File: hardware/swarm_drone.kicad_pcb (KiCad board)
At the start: 4 copper layers, 45 x 45 mm, 103 parts, among them J1 Conn_01x02_Pin, J2 Conn_01x03_Socket, J3 Conn_01x03_Socket, J5 Conn_01x02_Socket, J6 Conn_01x02_Socket, J7 Conn_01x02_Socket, J8 Conn_01x02_Socket, Q1 AO3400A, Q2 AO3400A, Q3 AO3400A, Q4 AO3400A, SW1 SW_Push, U1 STM32F405RGT7, U2 TPS7A91, U3 ICM-42688-P, U4 BMP581, U5 VL53L1CXV0FY1, U6 GD25Q128ESIGR, U7 nRF24L01P, X1 8MHz, Y1 16MHz (C13738)

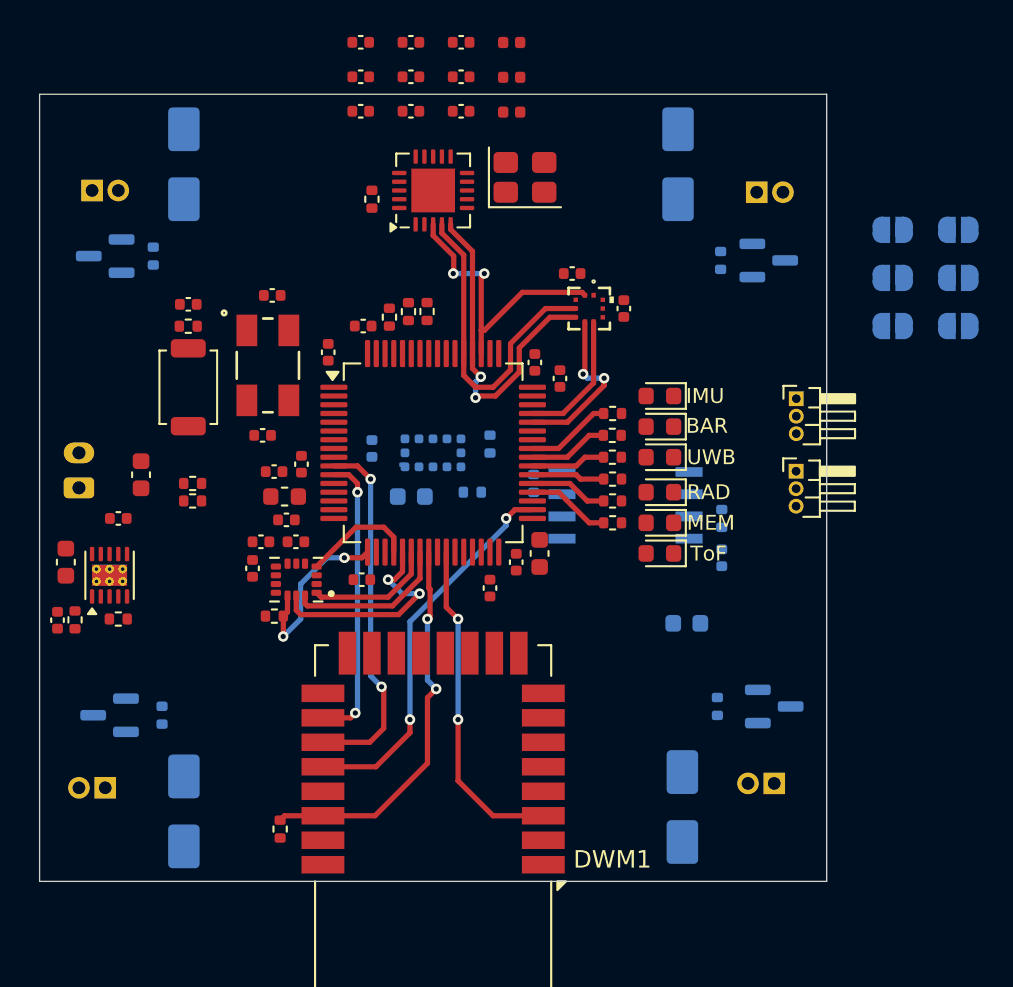
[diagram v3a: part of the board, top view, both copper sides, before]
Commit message: feat(kicad): Rerouted board and changed nets to provide ease in routing
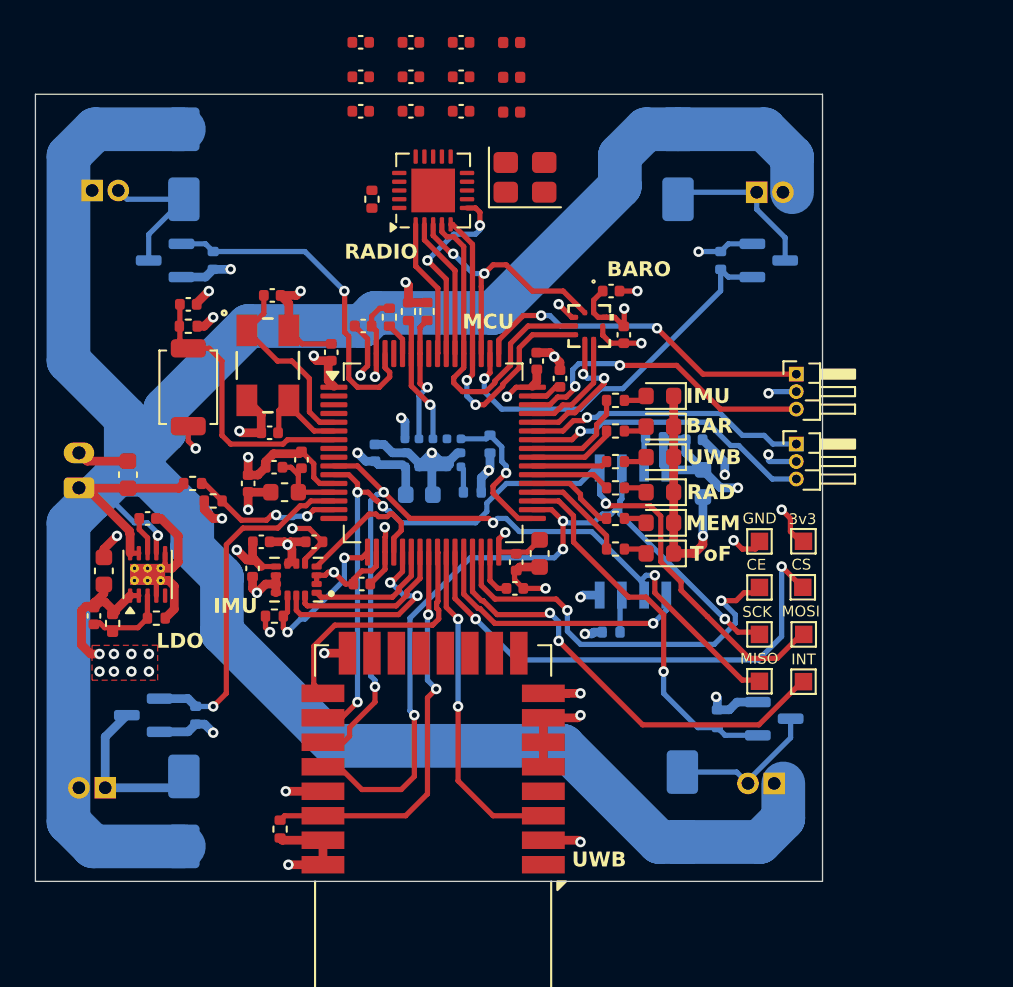
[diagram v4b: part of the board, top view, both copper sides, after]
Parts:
- removed JP1, JP2, JP3, JP4, JP5, JP6: Jumper_2_Open, Jumper:SolderJumper-2_P1.3mm_Open_RoundedPad1.0x1.5mm
- added TP1: MISO, TestPoint:TestPoint_Pad_1.0x1.0mm, F.Cu at (118.2, 76.3)
- added TP2: MOSI, TestPoint:TestPoint_Pad_1.0x1.0mm, F.Cu at (120.8, 73.6)
- added TP3: SCK, TestPoint:TestPoint_Pad_1.0x1.0mm, F.Cu at (118.2, 73.6)
- added TP4: CE, TestPoint:TestPoint_Pad_1.0x1.0mm, F.Cu at (118.2, 70.9)
- added TP5: CS, TestPoint:TestPoint_Pad_1.0x1.0mm, F.Cu at (120.7, 70.9)
- added TP6: INT, TestPoint:TestPoint_Pad_1.0x1.0mm, F.Cu at (120.7, 76.3)
- added TP7: +3v3, TestPoint:TestPoint_Pad_1.0x1.0mm, F.Cu at (120.7, 68.3)
- added TP8: GND, TestPoint:TestPoint_Pad_1.0x1.0mm, F.Cu at (118.2, 68.3)
- moved R19 9.58 mm to (109.8, 73.5), turned to 180 degrees
- moved C27 8.05 mm to (115.0, 65.0), turned to -90 degrees
- moved C26 6.93 mm to (114.5, 62.5), turned to 0 degrees
- moved R18 6.01 mm to (112.2, 62.4), turned to 180 degrees
- moved Q1 3.43 mm to (84.2, 52.2)
- moved R12 3.43 mm to (87.0, 52.2)
- moved C9 3.02 mm to (89.0, 65.0), turned to 90 degrees
- moved C20 2.44 mm to (109.8, 54.0), turned to 0 degrees
- moved C15 2.23 mm to (80.8, 70.0)
- moved R4 2.18 mm to (83.8, 72.7)
- moved U2 2.18 mm to (83.2, 70.2)
- moved R3 2.16 mm to (81.2, 73.0)
- moved C16 2.10 mm to (80.2, 72.6)
- moved Q4 1.92 mm to (83.0, 78.2)
- moved R15 1.92 mm to (86.0, 78.2)
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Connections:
- U1 pad 2: /Microcontroller/RADIO_ALT_CS -> unconnected-(U1-PC13-Pad2)
- U1 pad 27: unconnected-(U1-PB1-Pad27) -> /Microcontroller/RADIO_ALT_CS
- U1 pad 29: unconnected-(U1-PB10-Pad29) -> /Microcontroller/RADIO_ALT_INT
- U1 pad 3: /Microcontroller/RADIO_ALT_CE -> unconnected-(U1-PC14-Pad3)
- U1 pad 30: unconnected-(U1-PB11-Pad30) -> /Microcontroller/RADIO_ALT_CE
- U1 pad 4: /Microcontroller/RADIO_ALT_INT -> unconnected-(U1-PC15-Pad4)
- U1 pad 54: unconnected-(U1-PD2-Pad54) -> /Microcontroller/RADIO_CS
- U1 pad 57: /Microcontroller/RADIO_CS -> unconnected-(U1-PB5-Pad57)
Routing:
- net +BATT: track 0.00 -> 178.2 mm, vias 0 -> 1
- net GND: track 0.00 -> 125.1 mm, vias 0 -> 32
- net +3V3: track 0.00 -> 71.2 mm, vias 0 -> 27
- net /Flash Memory/SPI2_MOSI: track 16.7 -> 52.1 mm, vias 2 -> 4
- net /Microcontroller/RADIO_ALT_CS: track 0.00 -> 29.1 mm, vias 0 -> 2
- net /Flash Memory/SPI2_MISO: track 20.8 -> 48.2 mm, vias 2 -> 4
- net /Microcontroller/RADIO_ALT_INT: track 0.00 -> 26.1 mm, vias 0 -> 2
- net /Flash Memory/SPI2_SCK: track 22.0 -> 46.8 mm, vias 2 -> 4
- net /Microcontroller/RADIO_ALT_CE: track 0.00 -> 23.1 mm, vias 0 -> 2
- net /Microcontroller/M2: track 0.00 -> 22.3 mm, vias 0 -> 1
- net /Microcontroller/M3: track 0.00 -> 22.0 mm, vias 0 -> 1
- net /Microcontroller/M4: track 0.00 -> 20.0 mm, vias 0 -> 1
- net /Microcontroller/M1: track 0.00 -> 19.8 mm, vias 0 -> 1
- net /Microcontroller/SWCLK: track 0.00 -> 19.8 mm, vias 0 -> 2
- net /Microcontroller/SWDIO: track 0.00 -> 18.0 mm, vias 0 -> 2
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- added copper zone on F.Cu, net +3V3
- added copper zone on In2.Cu, net +3V3
- added copper zone on In1.Cu, net GND
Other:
- board text added: "3v3"
- board text added: "BARO"
- board text added: "CE"
- board text added: "CS"
- board text added: "GND"
- board text added: "INT"
- board text added: "LDO"
- board text added: "MCU"
- board text added: "MISO"
- board text added: "MOSI"
- board text added: "Memory"
- board text added: "RADIO"
- board text added: "SCK"
- board text added: "Tof"

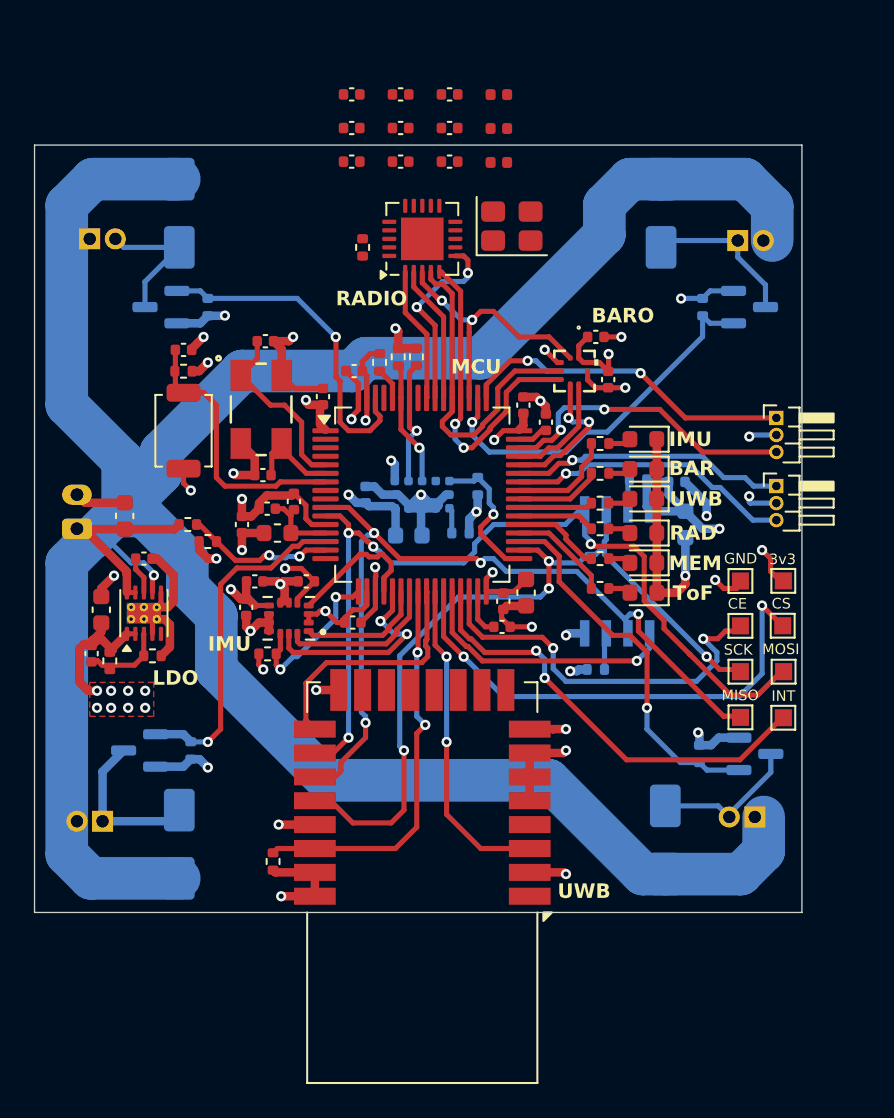
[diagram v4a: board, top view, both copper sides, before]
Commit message: feat(kicad): Updated via  spacing to prevent cutting up the ground plane
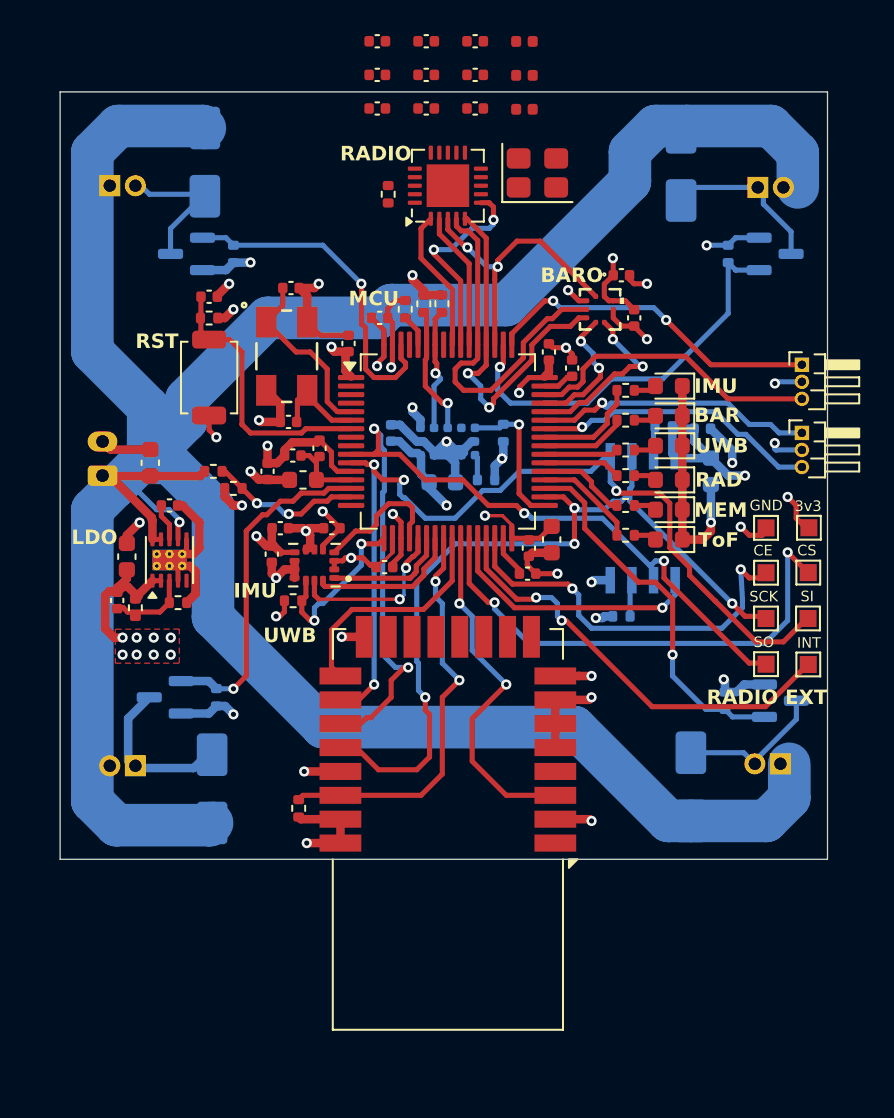
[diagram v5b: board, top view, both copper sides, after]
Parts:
- moved C21 3.92 mm to (112.0, 52.9)
- moved C20 3.92 mm to (111.2, 50.4)
- moved C24 3.92 mm to (97.8, 59.6)
- moved U4 3.92 mm to (110.0, 52.4)
- moved D4 3.78 mm to (87.2, 80.5)
- moved J8 3.78 mm to (82.0, 80.8)
- moved C2 3.75 mm to (97.4, 67.5)
- moved C25 3.69 mm to (100.8, 62.5)
- moved C12 3.53 mm to (108.4, 55.8)
- moved C11 3.46 mm to (105.8, 67.9)
- moved C15 3.46 mm to (82.2, 66.9)
- moved C19 3.46 mm to (90.8, 66.7)
- moved C5 3.46 mm to (105.8, 66.4)
- moved C6 3.46 mm to (107.2, 65.9)
- moved C7 3.46 mm to (92.0, 61.0)
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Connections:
- U1 pad 44: /Barometer/BARO_CS -> /Barometer/BARO_INT
- U1 pad 45: /Barometer/BARO_INT -> /Barometer/BARO_CS
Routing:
- net /Flash Memory/SPI2_MISO: track 48.2 -> 54.2 mm
- net /Barometer/BARO_INT: track 6.71 -> 10.5 mm, vias 0 -> 2
- net +3V3: track 71.2 -> 74.6 mm
- net /Barometer/SPI3_MISO: track 19.3 -> 21.6 mm
- net /Barometer/SPI3_MOSI: track 19.6 -> 21.7 mm
- net /IMU/SPI1_SCK: track 12.3 -> 10.2 mm
- net /Microcontroller/UWB_RESET: track 19.1 -> 20.8 mm
- net /Flash Memory/SPI2_MOSI: track 52.1 -> 53.8 mm
- net /Flash Memory/SPI2_SCK: track 46.8 -> 48.5 mm
- net /Microcontroller/M2: track 22.3 -> 23.8 mm
- net +BATT: track 178.2 -> 177.2 mm
- net GND: track 125.1 -> 126.2 mm
- net /Microcontroller/UWB_CS: track 14.6 -> 13.7 mm
- net /Microcontroller/RADIO_INT: track 11.3 -> 12.2 mm
- net /Barometer/SPI3_SCK: track 16.2 -> 17.0 mm
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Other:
- board text added: "RADIO EXT"
- board text added: "RST"
- board text added: "SI"
- board text added: "SO"
- board text removed: "MISO"
- board text removed: "MOSI"

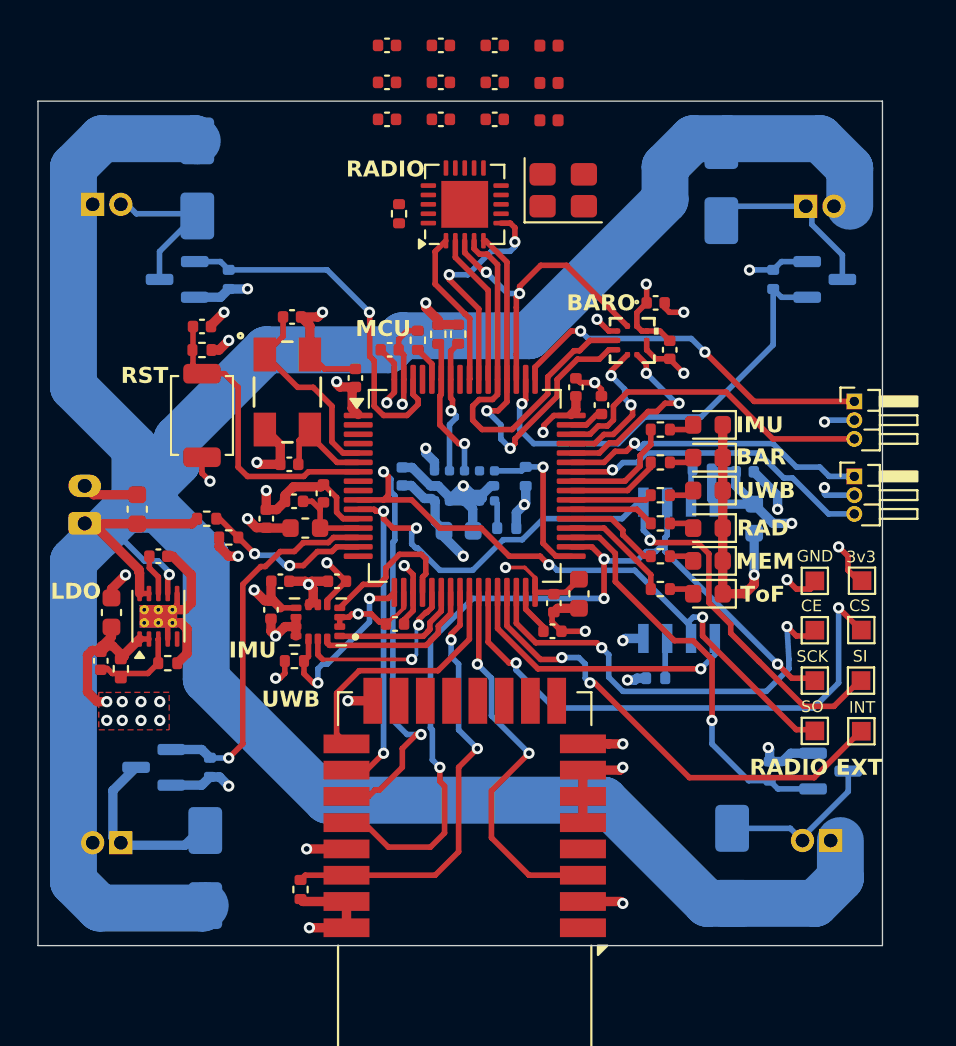
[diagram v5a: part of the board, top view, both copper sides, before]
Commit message: feat(kicad): Updated traces to reduce power plane slotting Finished inital pass of the NRF layout
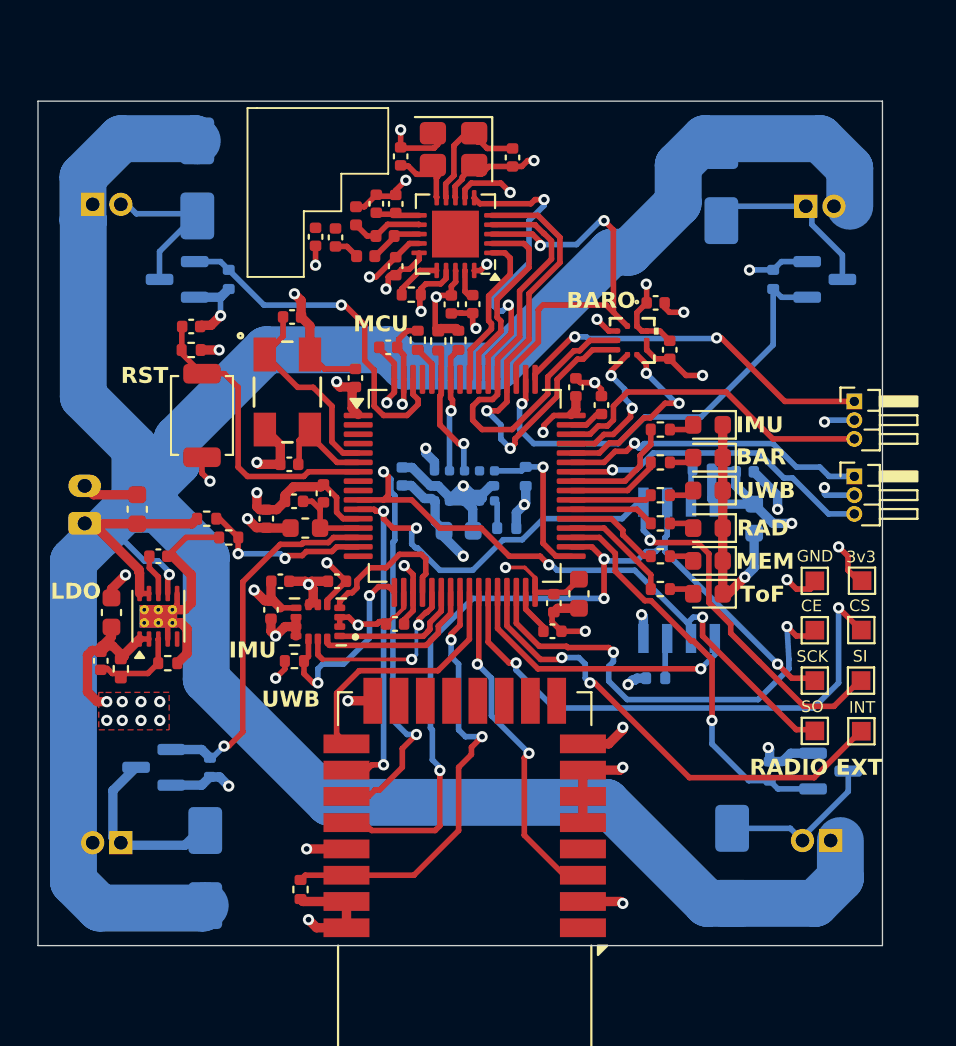
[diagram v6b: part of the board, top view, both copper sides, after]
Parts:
- moved C28 14.5 mm to (101.5, 50.5), turned to -90 degrees
- moved C34 14.0 mm to (93.1, 46.9), turned to 90 degrees
- moved L1 13.7 mm to (95.3, 45.7), turned to 90 degrees
- moved L2 13.4 mm to (95.8, 47.9), turned to 180 degrees
- moved L3 10.7 mm to (96.8, 46.8), turned to 180 degrees
- moved C30 10.4 mm to (100.4, 50.5), turned to -90 degrees
- moved C29 9.81 mm to (97.4, 48.4), turned to 90 degrees
- moved C31 8.78 mm to (97.4, 45.1), turned to 90 degrees
- moved C33 8.43 mm to (94.2, 46.9), turned to 90 degrees
- moved C32 7.33 mm to (96.4, 45.1), turned to 90 degrees
- moved Y1 6.24 mm to (100.5, 42.2), turned to 180 degrees
- moved C36 5.39 mm to (97.7, 42.6), turned to 90 degrees
- moved R20 4.36 mm to (98.2, 49.9), turned to 0 degrees
- moved C35 4.11 mm to (103.6, 42.6), turned to -90 degrees
- moved U7 1.66 mm to (100.6, 46.7), turned to 180 degrees
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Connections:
- net Net-(U7-ANT1) renamed /Radio/ANT1
- net Net-(U7-ANT2) renamed /Radio/ANT2
- net Net-(U7-DVDD) renamed /Radio/DVDD
- net Net-(U7-VDD_PA) renamed /Radio/VDD_PA
- U1 pad 54: /Microcontroller/RADIO_CS -> /Microcontroller/RADIO_INT
- U1 pad 55: /Microcontroller/RADIO_INT -> /Microcontroller/RADIO_CS
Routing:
- net GND: track 126.2 -> 153.6 mm, vias 32 -> 38
- net +3V3: track 74.6 -> 84.1 mm, vias 27 -> 29
- net Net-(U7-XC2): track 0.00 -> 6.85 mm
- net /Barometer/SPI3_MISO: track 21.6 -> 26.5 mm
- net /Barometer/SPI3_SCK: track 17.0 -> 21.5 mm
- net Net-(U7-XC1): track 0.00 -> 4.45 mm
- net /Microcontroller/RADIO_INT: track 12.2 -> 16.3 mm
- net /Barometer/SPI3_MOSI: track 21.7 -> 25.7 mm
- net /Radio/ANT1: track 0.00 -> 3.87 mm
- net /Radio/ANT2: track 0.00 -> 2.86 mm
- net Net-(U7-IREF): track 0.00 -> 2.58 mm
- net /Microcontroller/UWB_RESET: track 20.8 -> 18.2 mm
- net /Radio/VDD_PA: track 0.00 -> 2.43 mm
- net /Microcontroller/RADIO_CS: track 8.11 -> 10.3 mm
- net /Radio/DVDD: track 0.00 -> 1.62 mm
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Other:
- board text removed: "RADIO"
